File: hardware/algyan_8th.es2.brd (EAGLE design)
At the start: 142 x 55 mm, 43 parts, among them CN1 4P-2.0, U1 XIAO ESP32C3, U10 EC12E(Panel), U2 TM1640, U3 NJM2113M, U4 LTP-12188M-08, U5 NJM2113D, U6 UGSM23A, U7 EC12PLRVF, U8 TVGP01-G73BB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

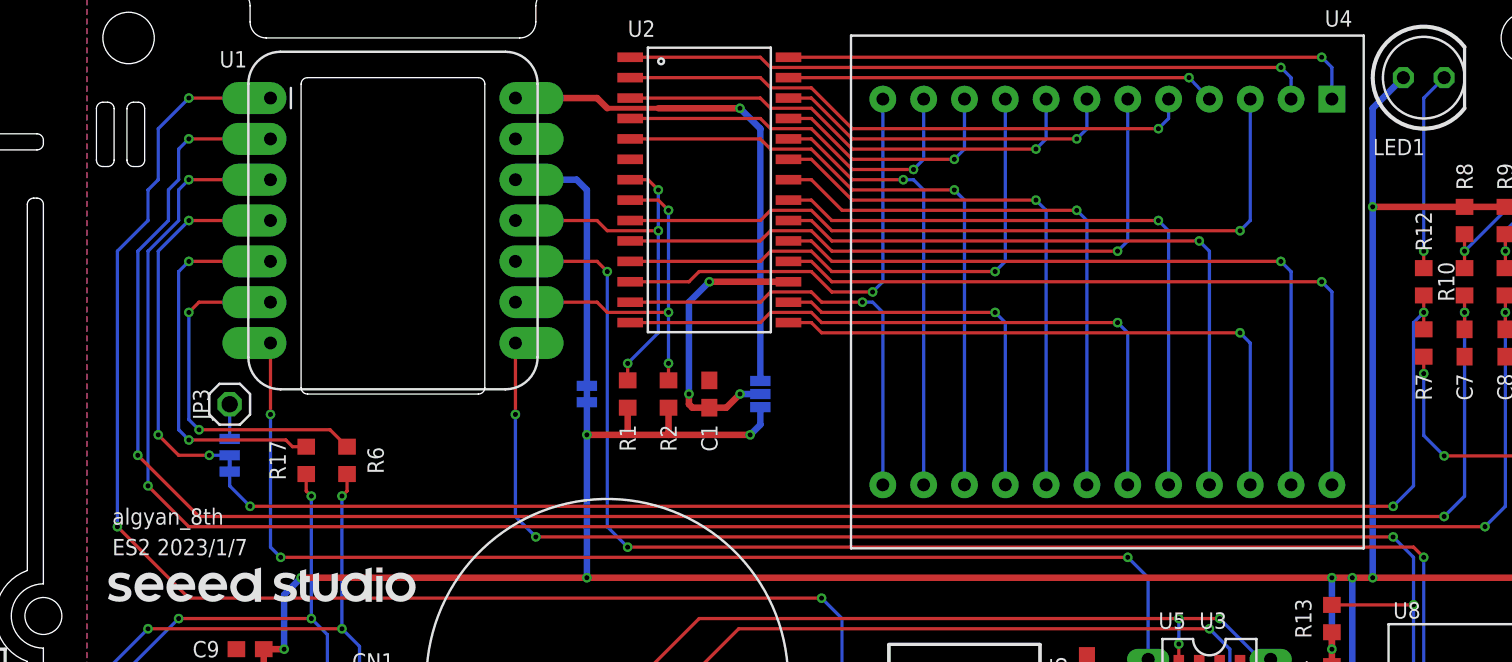
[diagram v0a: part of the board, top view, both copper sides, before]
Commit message: ES2基板のEAGLEファイルと回路図PDFを修正
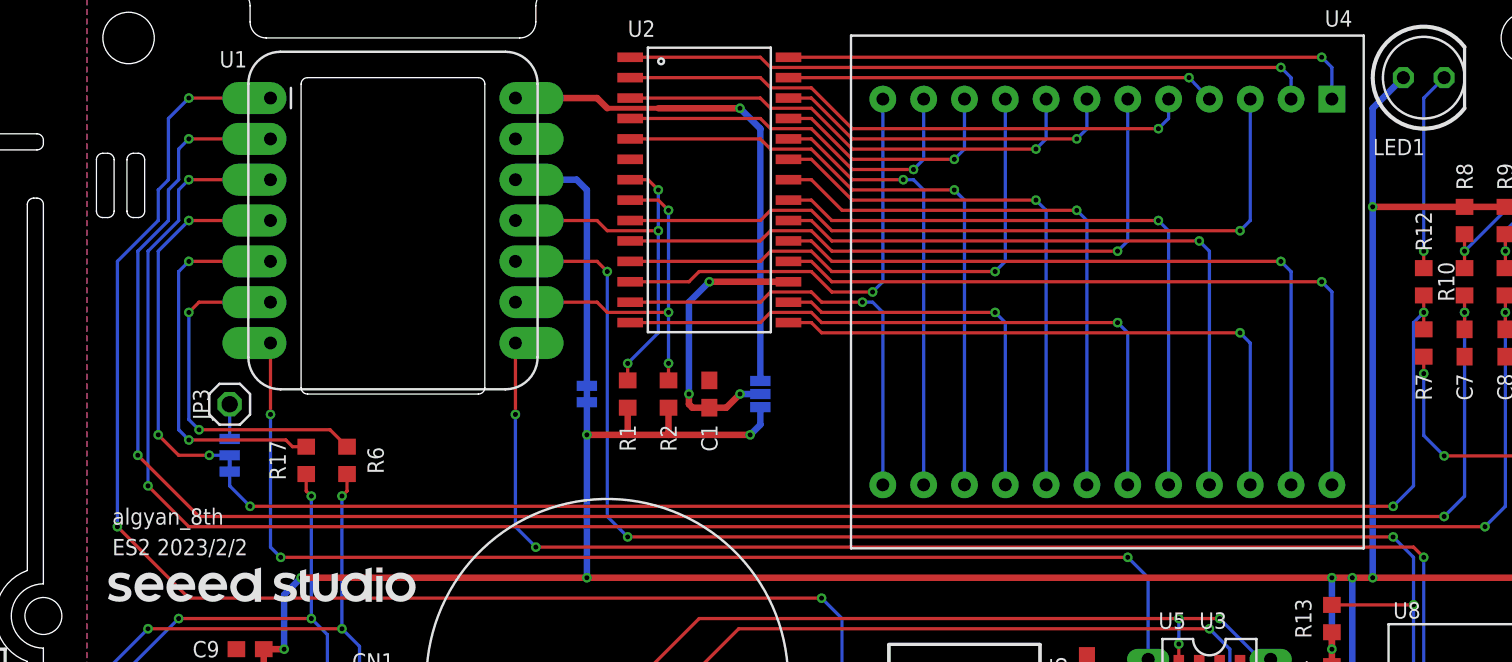
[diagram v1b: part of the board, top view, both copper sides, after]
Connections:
- net ESC-BTN: now also U1.8; no longer U1.10
- net N$2: now also U5.2
- net SEL-BTN: now also U1.10; no longer U1.8
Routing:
- net SEL-BTN: track 98.7 -> 103.4 mm
- net ESC-BTN: track 116.4 -> 111.6 mm
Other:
- outline, holes or cut-outs redrawn
- board text added: "ES2 2023/2/2"
- board text removed: "ES2 2023/1/7"
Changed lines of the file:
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@@
 <setting verticaltext="up"/>
 </settings>
-<grid distance="25" unitdist="mil" unit="mm" style="lines" multiple="4" display="yes" altdistance="0.025" altunitdist="inch" altunit="inch"/>
+<grid distance="25" unitdist="mil" unit="mil" style="lines" multiple="4" display="yes" altdistance="0.025" altunitdist="inch" altunit="inch"/>
 <layers>
 <layer number="1" name="Top" color="4" fill="1" visible="yes" active="yes"/>
@@
 <circle x="123.825" y="34.925" radius="17.5" width="0.2032" layer="48"/>
 <text x="26.9875" y="22.225" size="1.016" layer="21" font="vector" ratio="10" align="center-left">algyan_8th</text>
-<text x="26.9875" y="20.32" size="1.016" layer="21" font="vector" ratio="10" align="center-left">ES2 2023/1/7</text>
+<text x="26.9875" y="20.32" size="1.016" layer="21" font="vector" ratio="10" align="center-left">ES2 2023/2/2</text>
 <polygon width="0" layer="21">
 <vertex x="29.25955" y="18.73545"/>
@@
 <wire x1="139.065" y1="34.925" x2="123.825" y2="50.165" width="0" layer="20" curve="90"/>
 <wire x1="35.29" y1="4" x2="34.29" y2="3" width="0" layer="20" curve="90"/>
-<wire x1="26" y1="47.6" x2="26" y2="44.4" width="0" layer="20"/>
-<wire x1="26" y1="44.4" x2="26.4" y2="44" width="0" layer="20" curve="90"/>
-<wire x1="26.4" y1="44" x2="26.7" y2="44" width="0" layer="20"/>
-<wire x1="26.7" y1="44" x2="27.1" y2="44.4" width="0" layer="20" curve="90"/>
-<wire x1="27.1" y1="44.4" x2="27.1" y2="47.6" width="0" layer="20"/>
-<wire x1="27.1" y1="47.6" x2="26.7" y2="48" width="0" layer="20" curve="90"/>
-<wire x1="26.7" y1="48" x2="26.4" y2="48" width="0" layer="20"/>
-<wire x1="26.4" y1="48" x2="26" y2="47.6" width="0" layer="20" curve="90"/>
-<wire x1="28.3" y1="44" x2="28.6" y2="44" width="0" layer="20"/>
-<wire x1="28.6" y1="44" x2="29" y2="44.4" width="0" layer="20" curve="90"/>
-<wire x1="29" y1="44.4" x2="29" y2="47.6" width="0" layer="20"/>
-<wire x1="29" y1="47.6" x2="28.6" y2="48" width="0" layer="20" curve="90"/>
-<wire x1="28.6" y1="48" x2="28.3" y2="48" width="0" layer="20"/>
-<wire x1="28.3" y1="48" x2="27.9" y2="47.6" width="0" layer="20" curve="90"/>
-<wire x1="27.9" y1="47.6" x2="27.9" y2="44.4" width="0" layer="20"/>
-<wire x1="27.9" y1="44.4" x2="28.3" y2="44" width="0" layer="20" curve="90"/>
+<wire x1="26" y1="44.425" x2="26" y2="41.225" width="0" layer="20"/>
+<wire x1="26" y1="41.225" x2="26.4" y2="40.825" width="0" layer="20" curve="90"/>
+<wire x1="26.4" y1="40.825" x2="26.7" y2="40.825" width="0" layer="20"/>
+<wire x1="26.7" y1="40.825" x2="27.1" y2="41.225" width="0" layer="20" curve="90"/>
+<wire x1="27.1" y1="41.225" x2="27.1" y2="44.425" width="0" layer="20"/>
+<wire x1="27.1" y1="44.425" x2="26.7" y2="44.825" width="0" layer="20" curve="90"/>
+<wire x1="26.7" y1="44.825" x2="26.4" y2="44.825" width="0" layer="20"/>
+<wire x1="26.4" y1="44.825" x2="26" y2="44.425" width="0" layer="20" curve="90"/>
+<wire x1="28.3" y1="40.825" x2="28.6" y2="40.825" width="0" layer="20"/>
+<wire x1="28.6" y1="40.825" x2="29" y2="41.225" width="0" layer="20" curve="90"/>
+<wire x1="29" y1="41.225" x2="29" y2="44.425" width="0" layer="20"/>
+<wire x1="29" y1="44.425" x2="28.6" y2="44.825" width="0" layer="20" curve="90"/>
+<wire x1="28.6" y1="44.825" x2="28.3" y2="44.825" width="0" layer="20"/>
+<wire x1="28.3" y1="44.825" x2="27.9" y2="44.425" width="0" layer="20" curve="90"/>
+<wire x1="27.9" y1="44.425" x2="27.9" y2="41.225" width="0" layer="20"/>
+<wire x1="27.9" y1="41.225" x2="28.3" y2="40.825" width="0" layer="20" curve="90"/>
 <wire x1="50.165" y1="49.13" x2="50.165" y2="30.245" width="0" layer="20"/>
 <wire x1="50.165" y1="30.245" x2="49.765" y2="29.845" width="0" layer="20" curve="-90"/>
@@
 <contactref element="U3" pad="4"/>
 <wire x1="97.155" y1="6.4516" x2="97.155" y2="3.595" width="0.2032" layer="1"/>
+<contactref element="U5" pad="2"/>
+<wire x1="91.44" y1="5.715" x2="91.44" y2="10.795" width="0" layer="19" extent="1-1"/>
 </signal>
 <signal name="N$3">
@@
 <wire x1="71.12" y1="17.145" x2="31.75" y2="17.145" width="0.2032" layer="1"/>
 <wire x1="31.75" y1="17.145" x2="27.305" y2="21.59" width="0.2032" layer="1"/>
-<wire x1="27.305" y1="21.59" x2="27.305" y2="38.735" width="0.2032" layer="16"/>
-<wire x1="27.305" y1="38.735" x2="29.21" y2="40.64" width="0.2032" layer="16"/>
-<wire x1="29.21" y1="40.64" x2="29.21" y2="42.545" width="0.2032" layer="16"/>
-<wire x1="29.21" y1="42.545" x2="29.845" y2="43.18" width="0.2032" layer="16"/>
-<wire x1="29.845" y1="43.18" x2="29.845" y2="46.355" width="0.2032" layer="16"/>
-<wire x1="29.845" y1="46.355" x2="31.75" y2="48.26" width="0.2032" layer="16"/>
+<wire x1="27.305" y1="21.59" x2="27.305" y2="38.1" width="0.2032" layer="16"/>
+<wire x1="27.305" y1="38.1" x2="29.845" y2="40.64" width="0.2032" layer="16"/>
+<wire x1="29.845" y1="40.64" x2="29.845" y2="42.545" width="0.2032" layer="16"/>
+<wire x1="29.845" y1="42.545" x2="30.48" y2="43.18" width="0.2032" layer="16"/>
+<wire x1="30.48" y1="43.18" x2="30.48" y2="46.99" width="0.2032" layer="16"/>
+<wire x1="30.48" y1="46.99" x2="31.75" y2="48.26" width="0.2032" layer="16"/>
 <wire x1="31.75" y1="48.26" x2="36.83" y2="48.26" width="0.2032" layer="1"/>
 <via x="31.75" y="48.26" extent="1-16" drill="0.3048"/>
@@
 </signal>
 <signal name="SEL-BTN">
-<contactref element="U1" pad="8"/>
 <contactref element="U8" pad="3"/>
 <contactref element="U8" pad="4"/>
@@
 <wire x1="107.95" y1="16.725" x2="107.95" y2="19.685" width="0.2032" layer="16"/>
 <wire x1="107.95" y1="19.685" x2="106.68" y2="20.955" width="0.2032" layer="16"/>
-<wire x1="106.68" y1="20.955" x2="53.34" y2="20.955" width="0.2032" layer="1"/>
+<wire x1="106.68" y1="20.955" x2="59.055" y2="20.955" width="0.2032" layer="1"/>
 <wire x1="118.645" y1="7.025" x2="106.145" y2="7.025" width="0.2032" layer="1"/>
-<wire x1="53.34" y1="20.955" x2="52.07" y2="22.225" width="0.2032" layer="16"/>
-<wire x1="52.07" y1="22.225" x2="52.07" y2="28.575" width="0.2032" layer="16"/>
-<wire x1="52.07" y1="28.575" x2="52.07" y2="33.02" width="0.2032" layer="1"/>
-<via x="52.07" y="28.575" extent="1-16" drill="0.3048"/>
+<wire x1="59.055" y1="20.955" x2="57.785" y2="22.225" width="0.2032" layer="16"/>
+<wire x1="57.785" y1="22.225" x2="57.785" y2="37.465" width="0.2032" layer="16"/>
+<via x="57.785" y="37.465" extent="1-16" drill="0.3048"/>
 <via x="106.68" y="20.955" extent="1-16" drill="0.3048"/>
-<via x="53.34" y="20.955" extent="1-16" drill="0.3048"/>
+<via x="59.055" y="20.955" extent="1-16" drill="0.3048"/>
 <wire x1="102.87" y1="16.725" x2="107.95" y2="16.725" width="0.2032" layer="1"/>
 <via x="107.95" y="16.725" extent="1-16" drill="0.3048"/>
+<contactref element="U1" pad="10"/>
+<wire x1="57.785" y1="37.465" x2="57.15" y2="38.1" width="0.2032" layer="1"/>
+<wire x1="57.15" y1="38.1" x2="52.07" y2="38.1" width="0.2032" layer="1"/>
 </signal>
 <signal name="ESC-BTN">
-<contactref element="U1" pad="10"/>
 <contactref element="U9" pad="3"/>
 <contactref element="U9" pad="4"/>
@@
 <wire x1="108.585" y1="9.525" x2="108.585" y2="19.685" width="0.2032" layer="16"/>
 <wire x1="108.585" y1="19.685" x2="107.95" y2="20.32" width="0.2032" layer="1"/>
-<wire x1="107.95" y1="20.32" x2="59.055" y2="20.32" width="0.2032" layer="1"/>
-<wire x1="59.055" y1="20.32" x2="57.785" y2="21.59" width="0.2032" layer="16"/>
-<wire x1="57.785" y1="21.59" x2="57.785" y2="37.465" width="0.2032" layer="16"/>
-<wire x1="57.785" y1="37.465" x2="57.15" y2="38.1" width="0.2032" layer="1"/>
-<wire x1="57.15" y1="38.1" x2="52.07" y2="38.1" width="0.2032" layer="1"/>
-<via x="57.785" y="37.465" extent="1-16" drill="0.3048"/>
+<wire x1="107.95" y1="20.32" x2="53.34" y2="20.32" width="0.2032" layer="1"/>
+<wire x1="53.34" y1="20.32" x2="52.07" y2="21.59" width="0.2032" layer="16"/>
+<wire x1="52.07" y1="21.59" x2="52.07" y2="28.575" width="0.2032" layer="16"/>
+<via x="52.07" y="28.575" extent="1-16" drill="0.3048"/>
 <via x="108.585" y="19.685" extent="1-16" drill="0.3048"/>
-<via x="59.055" y="20.32" extent="1-16" drill="0.3048"/>
+<via x="53.34" y="20.32" extent="1-16" drill="0.3048"/>
 <wire x1="105.41" y1="9.525" x2="108.585" y2="9.525" width="0.2032" layer="1"/>
 <via x="108.585" y="9.525" extent="1-16" drill="0.3048"/>
 <wire x1="102.87" y1="11.215" x2="103.72" y2="11.215" width="0.2032" layer="1"/>
 <wire x1="103.72" y1="11.215" x2="105.41" y2="9.525" width="0.2032" layer="1"/>
+<contactref element="U1" pad="8"/>
+<wire x1="52.07" y1="28.575" x2="52.07" y2="33.02" width="0.2032" layer="1"/>
 </signal>
 <signal name="N$12">

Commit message: Fix #25
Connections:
- net N$2: no longer U5.2
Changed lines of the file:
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@@
 <layer number="21" name="tPlace" color="7" fill="1" visible="yes" active="yes"/>
 <layer number="22" name="bPlace" color="7" fill="1" visible="yes" active="yes"/>
-<layer number="23" name="tOrigins" color="15" fill="1" visible="yes" active="yes"/>
-<layer number="24" name="bOrigins" color="15" fill="1" visible="yes" active="yes"/>
+<layer number="23" name="tOrigins" color="15" fill="1" visible="no" active="yes"/>
+<layer number="24" name="bOrigins" color="15" fill="1" visible="no" active="yes"/>
 <layer number="25" name="tNames" color="7" fill="1" visible="yes" active="yes"/>
 <layer number="26" name="bNames" color="7" fill="1" visible="yes" active="yes"/>
@@
 <contactref element="U3" pad="4"/>
 <wire x1="97.155" y1="6.4516" x2="97.155" y2="3.595" width="0.2032" layer="1"/>
-<contactref element="U5" pad="2"/>
-<wire x1="91.44" y1="5.715" x2="91.44" y2="10.795" width="0" layer="19" extent="1-1"/>
 </signal>
 <signal name="N$3">
